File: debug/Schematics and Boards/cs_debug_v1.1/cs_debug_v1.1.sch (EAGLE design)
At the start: 217 parts, among them J1 J-JTAG-CORTEX_SMD, J19 Solar, J3 HIROSE-DF40_50-PIN_CONNECTORS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, J5 J-WURTH-USBC, Q10 2N7002P, Q3 FDN340P, Q4 2N7002P, Q5 FDN340P, Q6 2N7002P, Q7 FDN340P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

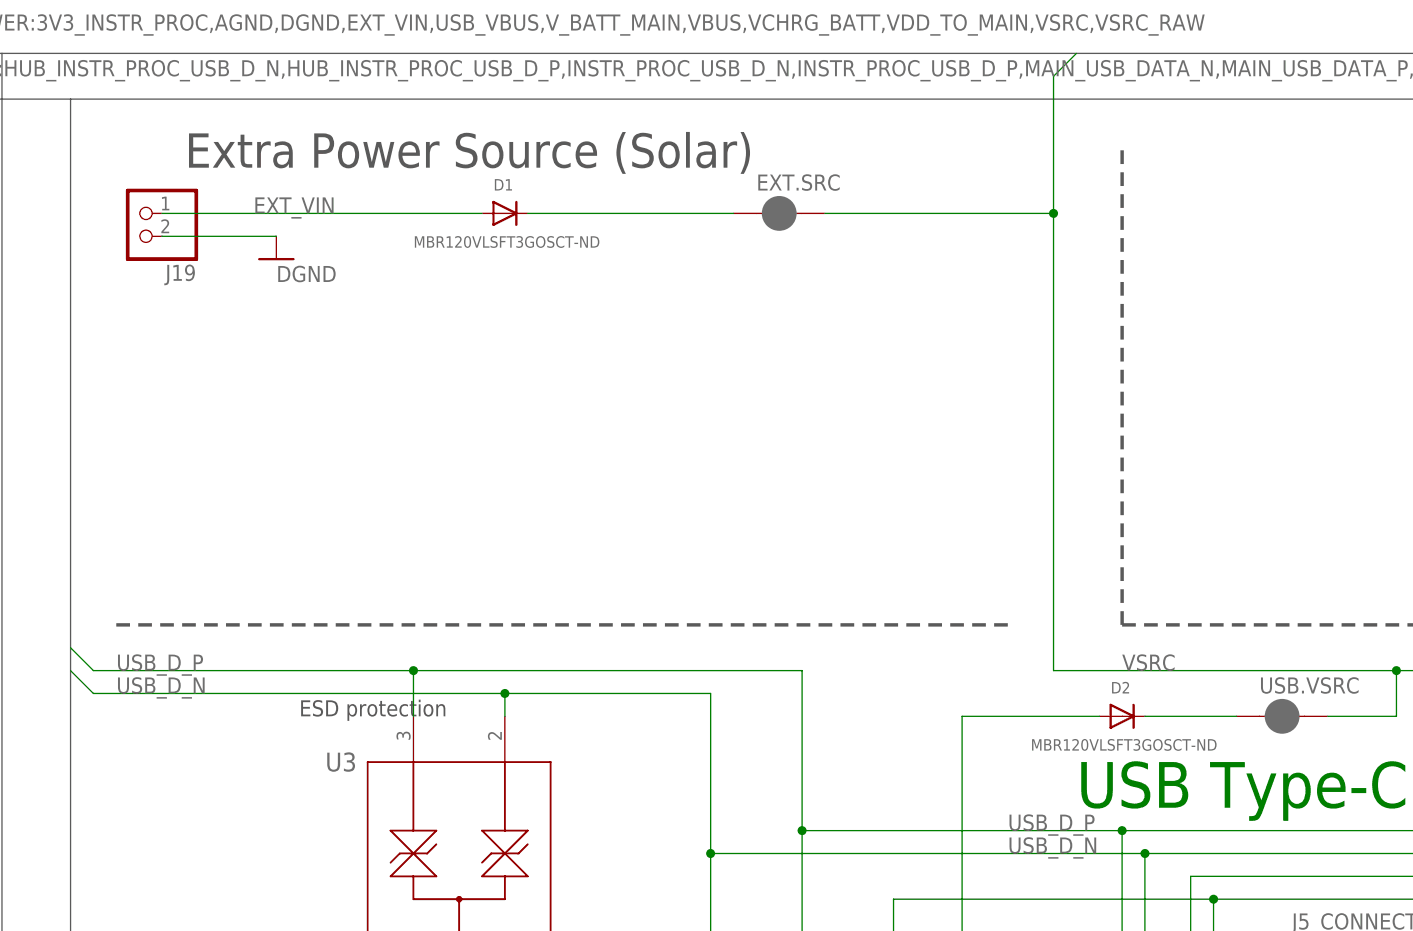
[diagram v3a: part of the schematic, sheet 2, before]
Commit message: DBG: Fix DFM issues for 7PCB
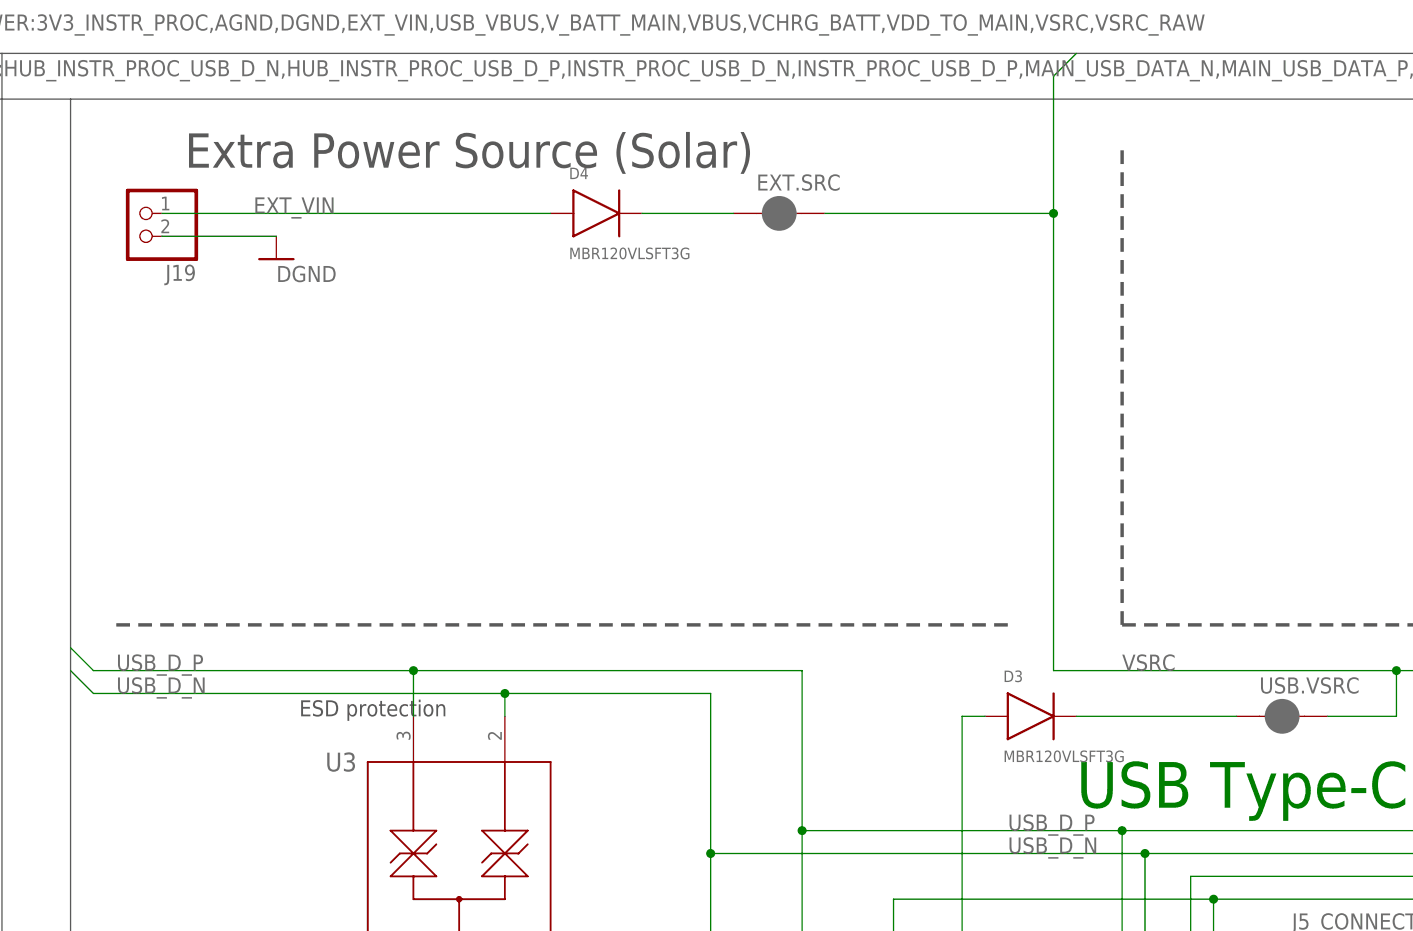
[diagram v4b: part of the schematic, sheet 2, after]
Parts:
- removed D1, D2: MBR120VLSFT3GOSCT-ND, adafruit:DIODESOD-123
- added D3, D4: MBR120VLSFT3G, Diodes:MBR120VLSFT3G
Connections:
- net EXT_VIN: now also D4.P; no longer D1.A
- net N$15: now also D4.N; no longer D1.C
- net USBC_VBUS: now also D3.P; no longer D2.A
- net VUSB_DIODE: now also D3.N; no longer D2.C
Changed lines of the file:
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@@
 <attribute name="PART_NO" value="S2B-PH-SM4-TB(LF)(SN)"/>
 </part>
-<part name="D1" library="adafruit" library_urn="urn:adsk.eagle:library:420" deviceset="DIODE" device="SOD-123" package3d_urn="urn:adsk.eagle:package:6240753/1" value="MBR120VLSFT3GOSCT-ND">
-<attribute name="MPN" value="MBR120VLSFT3G"/>
-<attribute name="PART_NO" value="MBR120VLSFT3G"/>
-</part>
 <part name="GND8" library="Supplies" deviceset="GND" device=""/>
 <part name="L1" library="SparkFun-Coils" deviceset="INDUCTOR" device="-0805-3.3UH" value="3.3µH/±20%/450mA">
@@
 <attribute name="PART_NO" value="MIC94164YCS-TR"/>
 </part>
-<part name="D2" library="adafruit" library_urn="urn:adsk.eagle:library:420" deviceset="DIODE" device="SOD-123" package3d_urn="urn:adsk.eagle:package:6240753/1" value="MBR120VLSFT3GOSCT-ND">
-<attribute name="MPN" value="MBR120VLSFT3G"/>
-<attribute name="PART_NO" value="MBR120VLSFT3G"/>
-</part>
 <part name="C.PHAT" library="Capacitors" deviceset="C-" device="1206" value="47u">
 <attribute name="MPN" value="C1206C476M8PACTU"/>
@@
 </part>
 <part name="SUPPLY13" library="Supplies" deviceset="+3V3" device=""/>
+<part name="D3" library="Diodes" deviceset="MBR120VLSFT3G" device=""/>
+<part name="D4" library="Diodes" deviceset="MBR120VLSFT3G" device=""/>
 </parts>
 <sheets>
@@
 <attribute name="PART_NO" x="27.94" y="406.4" size="1.778" layer="96" rot="R180" display="off"/>
 </instance>
-<instance part="D1" gate="G$1" x="68.58" y="406.4" smashed="yes">
-<attribute name="NAME" x="67.31" y="408.94" size="1.27" layer="95"/>
-<attribute name="VALUE" x="58.42" y="402.59" size="1.27" layer="96"/>
-<attribute name="MPN" x="68.58" y="406.4" size="1.778" layer="96" display="off"/>
-<attribute name="PART_NO" x="68.58" y="406.4" size="1.778" layer="96" display="off"/>
-</instance>
 <instance part="GND8" gate="1" x="43.18" y="401.32" smashed="yes"/>
 <instance part="L1" gate="G$1" x="215.9" y="355.6" smashed="yes" rot="R90">
@@
 <attribute name="PART_NO" x="236.22" y="307.34" size="1.778" layer="96" rot="R270" display="off"/>
 </instance>
-<instance part="D2" gate="G$1" x="137.16" y="350.52" smashed="yes">
-<attribute name="NAME" x="135.89" y="353.06" size="1.27" layer="95"/>
-<attribute name="VALUE" x="127" y="346.71" size="1.27" layer="96"/>
-<attribute name="MPN" x="137.16" y="350.52" size="1.778" layer="96" display="off"/>
-<attribute name="PART_NO" x="137.16" y="350.52" size="1.778" layer="96" display="off"/>
-</instance>
 <instance part="C.PHAT" gate="G$1" x="254" y="317.5" smashed="yes">
 <attribute name="NAME" x="255.016" y="319.405" size="1.778" layer="95"/>
@@
 </instance>
 <instance part="SUPPLY13" gate="G$1" x="220.98" y="208.28" smashed="yes"/>
+<instance part="D3" gate="G$1" x="127" y="350.52" smashed="yes">
+<attribute name="NAME" x="123.952" y="354.33" size="1.27" layer="95"/>
+<attribute name="VALUE" x="123.952" y="345.44" size="1.27" layer="96"/>
+</instance>
+<instance part="D4" gate="G$1" x="78.74" y="406.4" smashed="yes">
+<attribute name="NAME" x="75.692" y="410.21" size="1.27" layer="95"/>
+<attribute name="VALUE" x="75.692" y="401.32" size="1.27" layer="96"/>
+</instance>
 </instances>
 <busses>
@@
 <segment>
 <pinref part="J19" gate="G$1" pin="2"/>
-<pinref part="D1" gate="G$1" pin="A"/>
-<wire x1="30.48" y1="406.4" x2="66.04" y2="406.4" width="0.1524" layer="91"/>
+<wire x1="30.48" y1="406.4" x2="73.66" y2="406.4" width="0.1524" layer="91"/>
 <label x="40.64" y="406.4" size="1.778" layer="95"/>
+<pinref part="D4" gate="G$1" pin="P"/>
 </segment>
 </net>
@@
 <wire x1="119.38" y1="314.96" x2="119.38" y2="350.52" width="0.1524" layer="91"/>
 <junction x="119.38" y="314.96"/>
-<pinref part="D2" gate="G$1" pin="A"/>
-<wire x1="119.38" y1="350.52" x2="134.62" y2="350.52" width="0.1524" layer="91"/>
+<wire x1="119.38" y1="350.52" x2="121.92" y2="350.52" width="0.1524" layer="91"/>
+<pinref part="D3" gate="G$1" pin="P"/>
 </segment>
 <segment>
@@
 <net name="N$15" class="1">
 <segment>
-<pinref part="D1" gate="G$1" pin="C"/>
-<wire x1="71.12" y1="406.4" x2="93.98" y2="406.4" width="0.1524" layer="91"/>
 <pinref part="EXT.SRC" gate="G$1" pin="1"/>
+<wire x1="83.82" y1="406.4" x2="93.98" y2="406.4" width="0.1524" layer="91"/>
+<pinref part="D4" gate="G$1" pin="N"/>
 </segment>
 </net>
@@
 <net name="VUSB_DIODE" class="1">
 <segment>
-<pinref part="D2" gate="G$1" pin="C"/>
 <pinref part="USB.VSRC" gate="G$1" pin="1"/>
-<wire x1="139.7" y1="350.52" x2="149.86" y2="350.52" width="0.1524" layer="91"/>
+<wire x1="132.08" y1="350.52" x2="149.86" y2="350.52" width="0.1524" layer="91"/>
+<pinref part="D3" gate="G$1" pin="N"/>
 </segment>
 </net>

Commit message: DTR: Regen gerbers for final design fixes in rev2.1
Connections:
- removed net +3V3_INSTR_PROC: HUB.VDD.1
- net 3V3_INSTR_PROC: now also HUB.VDD.1
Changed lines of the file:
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@@
 <junction x="220.98" y="200.66"/>
+</segment>
+<segment>
+<pinref part="SUPPLY26" gate="G$1" pin="+3V3"/>
+<pinref part="HUB.VDD" gate="G$1" pin="1"/>
+<wire x1="114.3" y1="248.92" x2="114.3" y2="254" width="0.1524" layer="91"/>
+<label x="109.22" y="256.54" size="1.778" layer="95"/>
 </segment>
 </net>
@@
 </segment>
 </net>
-<net name="+3V3_INSTR_PROC" class="1">
-<segment>
-<pinref part="SUPPLY26" gate="G$1" pin="+3V3"/>
-<pinref part="HUB.VDD" gate="G$1" pin="1"/>
-<wire x1="114.3" y1="248.92" x2="114.3" y2="254" width="0.1524" layer="91"/>
-<label x="109.22" y="256.54" size="1.778" layer="95"/>
-</segment>
-</net>
